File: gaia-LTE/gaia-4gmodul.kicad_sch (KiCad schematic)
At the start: 24 parts, among them J1 4G antenna connector(U.FL), J6 Global Connector Technology S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, Q1 DTC143ZEBTL, Q3 DTC143ZEBTL, Q4 DTC143ZEBTL, U1 SIM7600E-H, U2 Gaia Connector A, U3 Gaia Connector B

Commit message: USB fix
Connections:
- net USB_DN: now also U3.15 (NC)
- net USB_DP: now also U3.16 (NC)
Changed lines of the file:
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@@
+		)
+	)
+	(label "USB_DP"
+		(at 40.64 207.01 180)
+		(effects
+			(font
+				(size 1.27 1.27)
+			)
+			(justify right bottom)
 		)
 	)
@@
 		(effects
 			(font
+				(size 1.27 1.27)
+			)
+			(justify left bottom)
+		)
+	)
+	(label "USB_DN"
+		(at 68.58 207.01 0)
+		(effects
+			(font

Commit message: -
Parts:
- removed C3: 100nF, Capacitor_SMD:C_0402_1005Metric, symbol Device:C_Small
- removed J6: Global Connector Technology SIM8060-6-0-14-00-A, Connector_Card:nanoSIM_GCT_SIM8060-6-0-14-00, symbol Connector:SIM_Card_Shielded
- removed R20: 0, Resistor_SMD:R_0603_1608Metric, symbol Device:R_Small
- added C15: 100nF, Capacitor_SMD:C_0603_1608Metric, symbol Device:C_Small
- added Q4: DTC143ZEBTL, gaia-4gmodul-footprints:DTC143ZEBTL, symbol gaia-4gmodul-symbols:DTC143ZEBTL
- U1: renamed from U2; footprint gaia-4gmodul-footprints:Gaia_connector_4_6layer -> gaia-4gmodul-footprints:Gaia_connector_2_4layer
- U2: renamed from U3; footprint gaia-4gmodul-footprints:Gaia_connector_4_6layer -> gaia-4gmodul-footprints:Gaia_connector_2_4layer
- renumbered C47 to C1, C20 to C2, C4 to C3, C18 to C4, C51 to C5, C2 to C6, C24 to C7, C50 to C8, C49 to C9, D2 to D1, D1 to D2, Q4 to Q1, Q1 to Q2, R12 to R1, R13 to R2, R19 to R4, U1 to U3
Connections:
- net GND: now also C15.2, Q4.2
- net reset_input: now also U1.12 (NC)
- net SD_CMD: now reaches U3.21 (SD_CMD)
- net SD_DAT0: now reaches U3.22 (SD_DATA0)
- net SD_DAT1: now reaches U3.23 (SD_DATA1)
- net SD_DAT2: now reaches U3.24 (SD_DATA2)
- net SD_DAT3: now reaches U3.25 (SD_DATA3)
- net SD_CLK: now reaches U3.26 (SD_CLK)
- net pwrkey: now reaches U3.3 (PWRKEY)
- net pwrkey: now also C15.1, Q4.3
- net pwrkey_input: now reaches U1.11 (NC)
- net pwrkey_input: now also Q4.1
- net +BATT: no longer names the net of U1.17 (+BATT)
- net +BATT: no longer U1.18 (+BATT)
- net -BATT: no longer names the net of U1.19 (-BATT)
- net -BATT: no longer U1.20 (-BATT)
- net EXP0_USART_RXD: no longer names the net of U2.13 (EXP2_USART_RXD)
- net EXP0_USART_TXD: no longer names the net of U2.11 (EXP2_USART_TXD)
- net EXP1_SPI_CS: no longer names the net of U2.6 (EXP1_SPI_CS)
- net EXP2_USART_RXD: no longer names the net of U2.14 (EXP2_USART_RXD)
- net EXP2_USART_TXD: no longer names the net of U2.12 (EXP2_USART_TXD)
- net I2C_1_SCL: no longer names the net of U2.3 (I2C_1_SCL)
- net I2C_1_SDA: no longer names the net of U2.1 (I2C_1_SCL)
- net I2C_2_SCL: no longer names the net of U2.4 (I2C_2_SCL)
- net I2C_2_SDA: no longer names the net of U2.2 (I2C_2_SDA)
- net SPI_0_MISO: no longer names the net of U2.5 (SPI_0_MISO)
- net SPI_0_MOSI: no longer names the net of U2.7 (SPI_0_MOSI)
- net SPI_0_SCLK: no longer names the net of U2.9 (SPI_0_SCLK)
- net VOUT_A1: no longer names the net of U1.1 (VOUT_A1)
- net VOUT_A1: no longer U1.2 (VOUT_A1)
- net VOUT_A2: no longer names the net of U1.4 (VOUT_A2)
- net VOUT_A2: no longer U1.3 (VOUT_A2)
- net VOUT_A3: no longer names the net of U1.5 (VOUT_A3)
- net VOUT_A3: no longer U1.6 (VOUT_A3)
- net VOUT_B1: no longer names the net of U1.7 (VOUT_B1)
- net VOUT_B1: no longer U1.8 (VOUT_B1)
- net VOUT_B2 renamed Vbat
- net Vbat: now also U1.3 (VOUT_A2); no longer U1.10 (VOUT_B2), U1.9 (VOUT_B2)
- no-connect marks 51 -> 69
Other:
- added sheet sdCard (sdcard.kicad_sch)
- added sheet simCard (simcard.kicad_sch)
- note added: "PWRKEY"
- note added: "SD card"
- moved on the sheet: C1, C2, C3, C4, C5, C6, C7, C8, C9, D1, D2, J1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

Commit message: preparing to install TVS
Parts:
- added C16, C17: NM_NC, Capacitor_SMD:C_0402_1005Metric, symbol Device:C_Small
- added J2: AUX Ant connector(u.fl), Connector_Coaxial:U.FL_Hirose_U.FL-R-SMT-1_Vertical, symbol Connector:Conn_Coaxial_Small
- added R3: 0, Resistor_SMD:R_0402_1005Metric, symbol Device:R_Small
- added TP1: TestPoint, TestPoint:TestPoint_Pad_1.5x1.5mm, symbol Connector:TestPoint
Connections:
- net GND: now also C16.1, C17.2, J2.2 (Ext)
- net Vbat: no longer C5.1, C6.1, C7.1, D1.2 (A), D2.2 (A), U1.3 (VOUT_A2), U3.11 (USB_VBUS), U3.62 (VBAT), U3.63 (VBAT)
- net at U3.59 (AUX_ANT): now also C16.2, R3.1
- net at U3.85 (BOOT_CFG0): now also TP1.1
- new net: C17.1, J2.1 (In), R3.2
- new net VBUS: C5.1, C6.1, C7.1, D1.2 (A), D2.2 (A), U1.3 (VOUT_A2), U3.11 (USB_VBUS), U3.62 (VBAT), U3.63 (VBAT)
- no-connect marks 69 -> 67
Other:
- moved on the sheet: C2, C3, C4, C5, C6, C7, C8, C9, J1, R4, U3

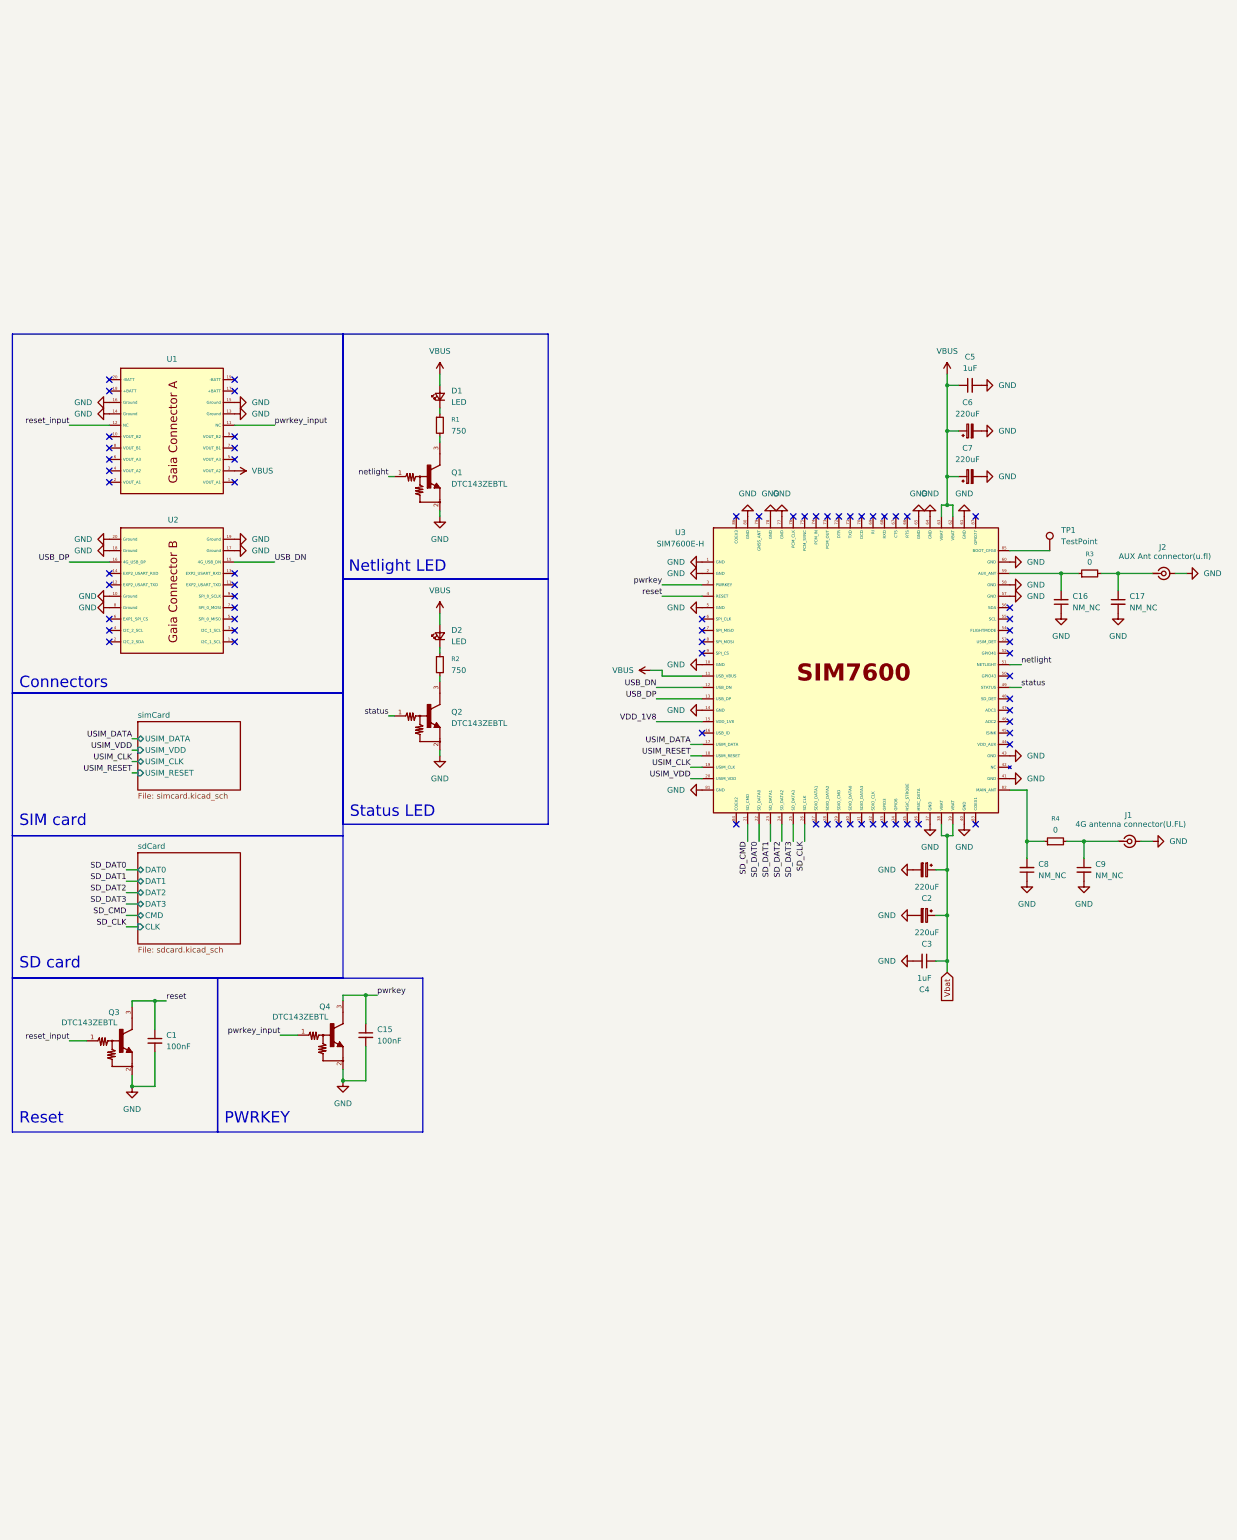
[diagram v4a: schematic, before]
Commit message: adding TVS diodes 1/2
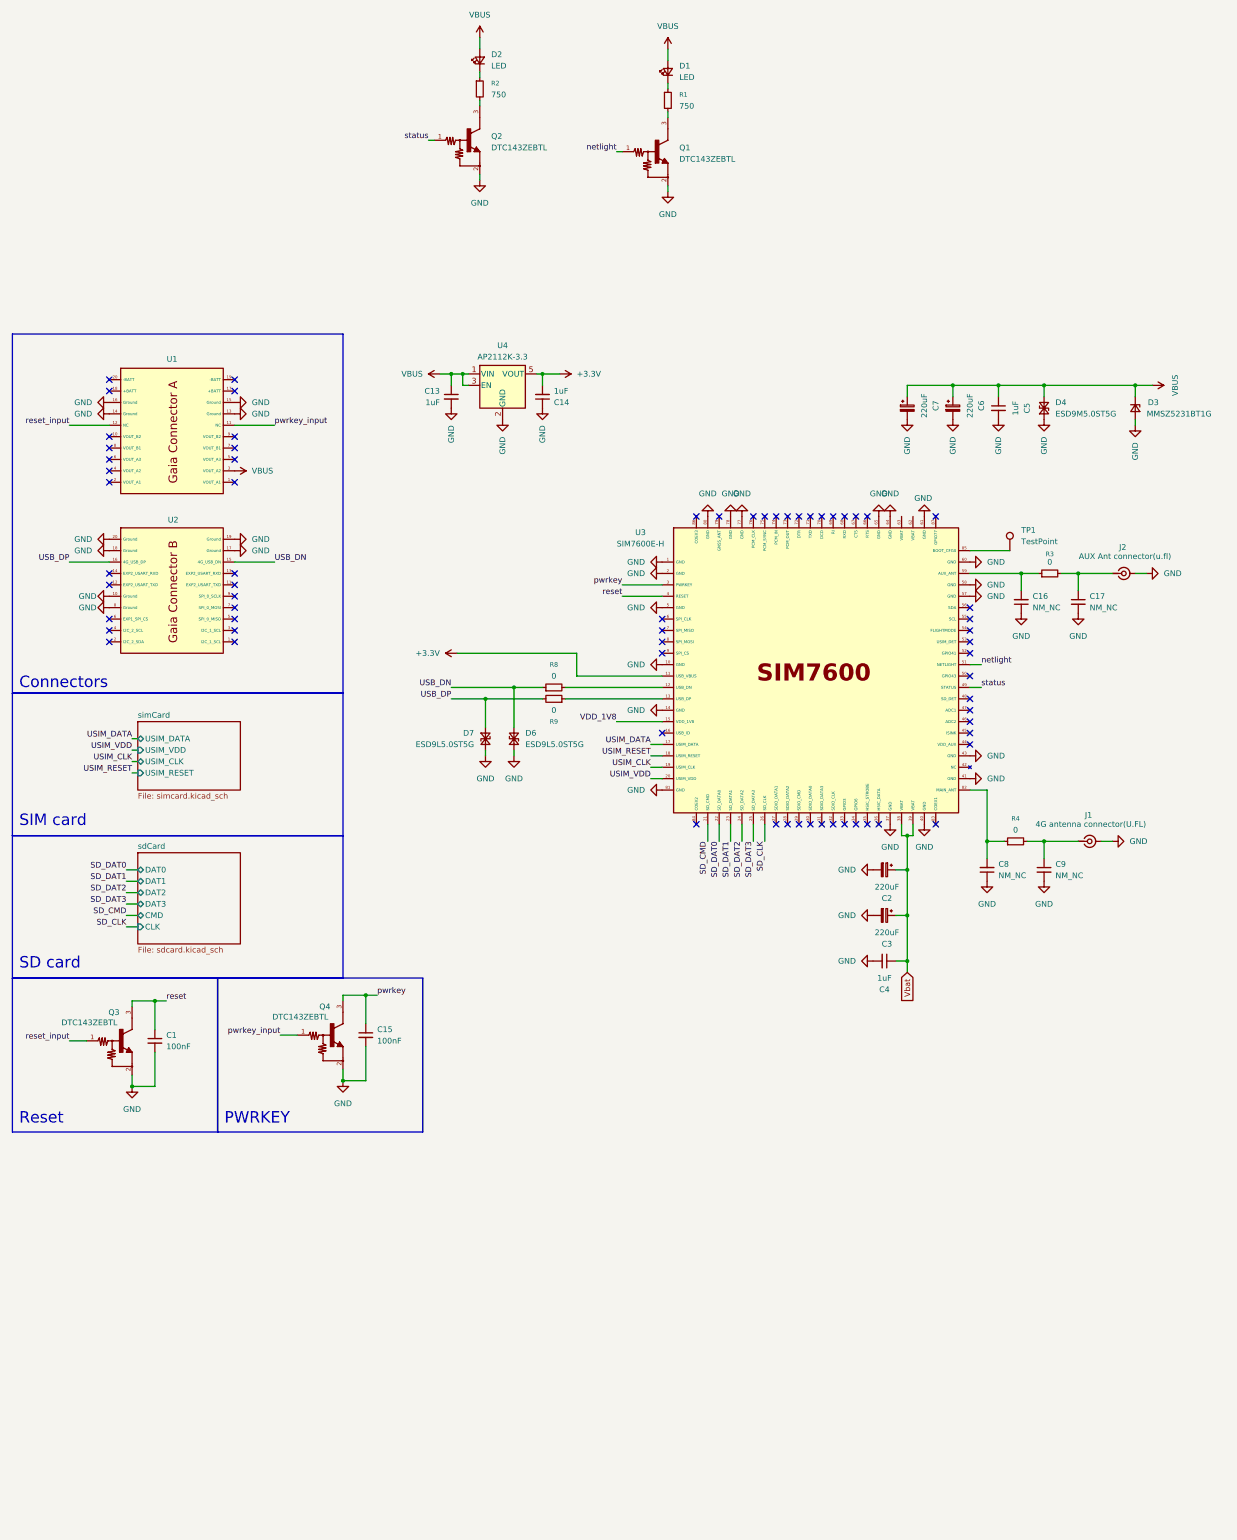
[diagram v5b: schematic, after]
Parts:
- added C13, C14: 1uF, symbol Device:C_Small
- added D3: MMSZ5231BT1G, symbol Device:D_Zener_Small
- added D4: ESD9M5.0ST5G, Diode_SMD:D_SOD-923, symbol Device:D_TVS_Small
- added D6, D7: ESD9L5.0ST5G, Diode_SMD:D_SOD-923, symbol Device:D_TVS_Small
- added R8, R9: 0, Resistor_SMD:R_0402_1005Metric, symbol Device:R_Small
- added U4: AP2112K-3.3, Package_TO_SOT_SMD:SOT-23-5, symbol Regulator_Linear:AP2112K-3.3
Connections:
- net GND: now also C13.2, C14.1, D3.2 (A), D4.1 (A1), D6.1 (A1), D7.2 (A2), U4.2 (GND)
- net USB_DN: now also D6.2 (A2), R8.1; no longer U3.12 (USB_DN)
- net USB_DP: now also D7.1 (A1), R9.2; no longer U3.13 (USB_DP)
- net VBUS: now also C13.1, D3.1 (K), D4.2 (A2), U4.1 (VIN), U4.3 (EN); no longer U3.11 (USB_VBUS), U3.62 (VBAT), U3.63 (VBAT)
- new net: R8.2, U3.12 (USB_DN)
- new net: R9.1, U3.13 (USB_DP)
- new net +3.3V: C14.2, U3.11 (USB_VBUS), U4.5 (VOUT)
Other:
- note removed: "Netlight LED"
- note removed: "Status LED"
- moved on the sheet: C16, C17, C2, C3, C4, C5, C6, C7, C8, C9, D1, D2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

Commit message: schematic arragements
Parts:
- removed C14: 1uF, symbol Device:C_Small
- removed C2, C3: 220uF, Capacitor_SMD:CP_Elec_5x5.9, symbol Device:C_Polarized_Small
- removed U1: Gaia Connector A, gaia-4gmodul-footprints:Gaia_connector_2_4layer, symbol gaia-4gmodul-symbols:gaia-2/4layer-connectorA
- removed U2: Gaia Connector B, gaia-4gmodul-footprints:Gaia_connector_2_4layer, symbol gaia-4gmodul-symbols:gaia-2/4layer-connectorB
- removed U4: AP2112K-3.3, Package_TO_SOT_SMD:SOT-23-5, symbol Regulator_Linear:AP2112K-3.3
- added C10, C3: 1uF, Capacitor_SMD:C_1812_4532Metric, symbol Device:C_Small
- added C11: 100nF, Capacitor_SMD:C_0603_1608Metric, symbol Device:C_Small
- added C12: 100nF, Capacitor_SMD:C_0402_1005Metric, symbol Device:C_Small
- added C14, C18: 220uF, Capacitor_SMD:CP_Elec_5x5.9, symbol Device:C_Polarized_Small
- added C2: 4.7uF, Capacitor_SMD:C_0603_1608Metric, symbol Device:C_Small
- added D10, D11, D12, D13, D14, D5, D9: ESD9M5, Diode_SMD:D_SOD-923, symbol Device:D_TVS_Small
- added D8: ESDA6V1W5, Package_TO_SOT_SMD:SOT-23-5, symbol Power_Protection:ESDA6V1SC5
- added J4: Micro_SD_Card_Det2, Connector_Card:microSD_HC_Hirose_DM3D-SF, symbol Connector:Micro_SD_Card_Det2
- added J5: SIM8051-6-0-14-00-A_REVD6, gaia-4gmodul-footprints:GCT_SIM8051-6-0-14-00-A_REVD6, symbol gaia-4gmodul-symbols:SIM8051-6-0-14-00-A_REVD6
- added J6, J7: Conn_02x10_Odd_Even, gaia_obc-footprints:PinHeader_2x10_P2.00mm_Vertical_SMD, symbol Connector_Generic:Conn_02x10_Odd_Even
- added R10, R11, R12: 22R, symbol Device:R_Small
- added U1: AP2127K-2.8, Package_TO_SOT_SMD:SOT-23-5, symbol Regulator_Linear:AP2127K-2.8
- C13: footprint (none) -> Capacitor_SMD:C_1812_4532Metric
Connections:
- net +3.3V is gone; now on net VBUS: U3.11 (USB_VBUS)
- net Vbat is gone; now on net VBUS: C4.1, U3.38 (VBAT), U3.39 (VBAT)
- net GND: now also C10.2, C11.1, C12.2, C14.2, C18.2, C2.2, C3.2, D10.1 (A1), D11.1 (A1), D12.1 (A1), D13.1 (A1), D14.1 (A1), D5.1 (A1), D8.2 (A), D9.1 (A1), J4.11 (SHIELD), J4.6 (VSS), J5.4 (SHIELD), J5.5 (GND), J5.8 (SHIELD), J6.17 (Pin_17), J6.18 (Pin_18), J6.19 (Pin_19), J6.20 (Pin_20), J7.13 (Pin_13), J7.14 (Pin_14), J7.15 (Pin_15), J7.16 (Pin_16), U1.2 (GND)
- net SD_CLK: now also D10.2 (A2), J4.5 (CLK)
- net SD_CMD: now also D11.2 (A2), J4.3 (CMD)
- net SD_DAT0: now also D9.2 (A2), J4.7 (DAT0)
- net SD_DAT1: now also D5.2 (A2), J4.8 (DAT1)
- net SD_DAT2: now also D13.2 (A2), J4.1 (DAT2)
- net SD_DAT3: now also D12.2 (A2), J4.2 (DAT3/CD)
- net USB_DN: now also J6.15 (Pin_15)
- net USB_DP: now also J6.16 (Pin_16)
- net USIM_CLK: now also D8.4 (K), R11.1
- net USIM_DATA: now also D8.5 (K), R12.1
- net USIM_RESET: now also D8.3 (K), R10.1
- net USIM_VDD: now also C11.2, D8.1 (K), J5.1 (VCC)
- net VBUS: now also U3.62 (VBAT), U3.63 (VBAT), C14.1, C18.1, C3.1, J7.3 (Pin_3), U1.1 (VIN), U1.3 (EN)
- net pwrkey_input: now also J7.11 (Pin_11)
- net reset_input: now also J7.12 (Pin_12)
- net VDD_1V8: no longer names the net of U3.15 (VDD_1V8)
- net netlight: no longer names the net of Q1.1, U3.51 (NETLIGHT)
- net pwrkey: no longer names the net of C15.1, Q4.3, U3.3 (PWRKEY)
- net reset: no longer names the net of C1.1, Q3.3, U3.4 (RESET)
- net status: no longer names the net of Q2.1, U3.49 (STATUS)
- new net: J5.2 (RST), R10.2
- new net: J5.3 (CLK), R11.2
- new net: J5.7 (I/O), R12.2
- new net +2V8: C10.1, C12.1, C2.1, D14.2 (A2), J4.4 (VDD), U1.5 (VOUT)
- no-connect marks 67 -> 45
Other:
- removed sheet sdCard
- removed sheet simCard
- note removed: "Connectors"
- note removed: "PWRKEY"
- note removed: "Reset"
- note removed: "SD card"
- note removed: "SIM card"
- company: OnionSAT -> (none)
- title: CS26 4G modul root -> GAIA LTE Module
- moved on the sheet: C1, C15, C16, C17, C4, C5, C6, C7, C8, C9, D1, D2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
